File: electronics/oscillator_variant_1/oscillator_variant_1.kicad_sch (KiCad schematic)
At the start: 48 parts, among them J1 module_2x15_left_input, J2 module_2x15_right_input, J3 Coax, Q1 BC337, U1 TL081, U2 LME49720, U3 TL082, U4 TL431

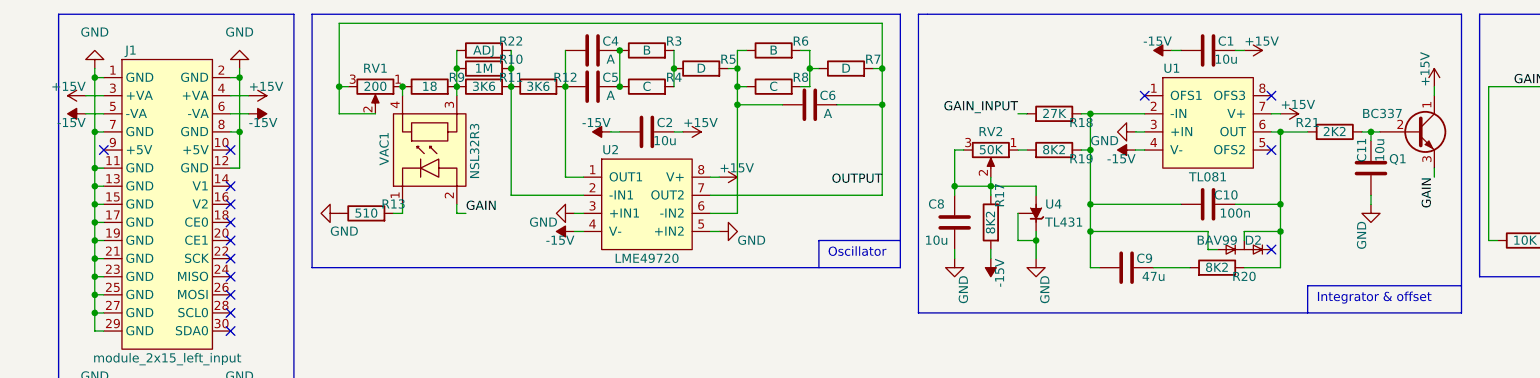
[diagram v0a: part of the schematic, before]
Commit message: placing and routing in progress, changed some ordering of resistors
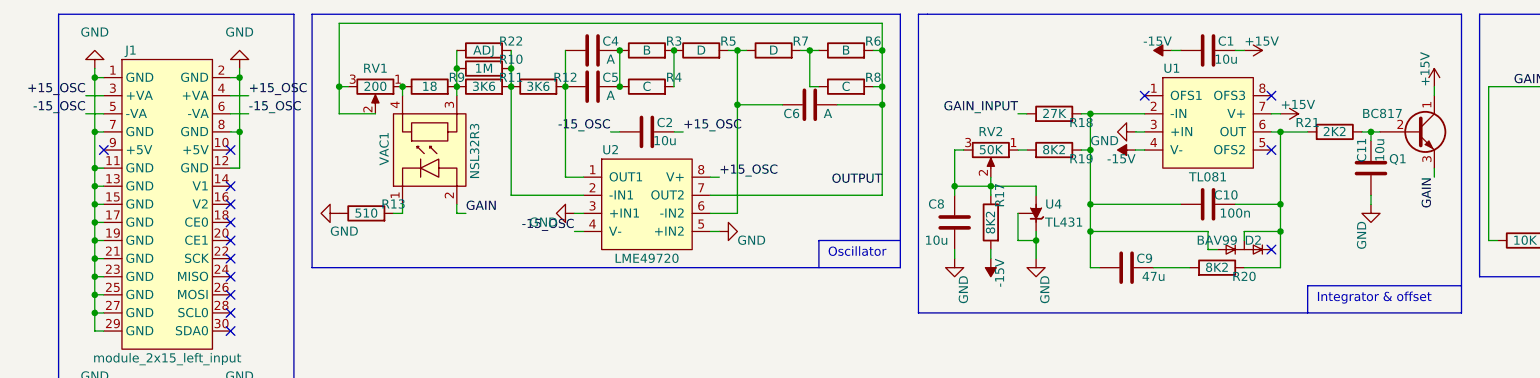
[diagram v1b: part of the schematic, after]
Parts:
- C10, C9: footprint SquantorRcl:C-025_050-030X100-film -> SquantorRcl:C-050-030X100-film
- C4, C5, C6: footprint SquantorRcl:C-025_050-030X100-film -> SquantorRcl:C-025_050-050X100-0805-3516-film
- Q1: value BC337 -> BC817; footprint Package_TO_SOT_THT:TO-92L_Inline_Wide -> SquantorIC:SOT23-3
- RV2: footprint Potentiometer_THT:Potentiometer_Bourns_3296W_Vertical -> SquantorRcl:POT_ALPS_RK09K111
- U4: footprint Package_TO_SOT_THT:TO-92_Inline_Wide -> SquantorIC:SOT23-3
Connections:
- net +15V: no longer C2.2, J1.3 (+VA), J1.4 (+VA), U2.8 (V+)
- net -15V: no longer C2.1, J1.5 (-VA), J1.6 (-VA), U2.4 (V-)
- net OUTPUT: now also R6.2, R8.2; no longer R7.2
- net at C6.1, R5.2, U2.6 (-IN2): now also R7.1; no longer R6.1, R8.1
- new net: R6.1, R7.2, R8.1
- new net +15_OSC: C2.2, J1.3 (+VA), J1.4 (+VA), U2.8 (V+)
- new net -15_OSC: C2.1, J1.5 (-VA), J1.6 (-VA), U2.4 (V-)
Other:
- moved on the sheet: R5, R6, R7, R8

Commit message: placing and routing further
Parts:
- R1, R13, R14, R15, R16, R17, R18, R19, R2, R20, R21: footprint SquantorRcl:R_0805+0603 -> SquantorRcl:R_0603_hand
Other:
- note added: "Power flags"
- note added: "interfaces"
- moved on the sheet: J3, R1, R2

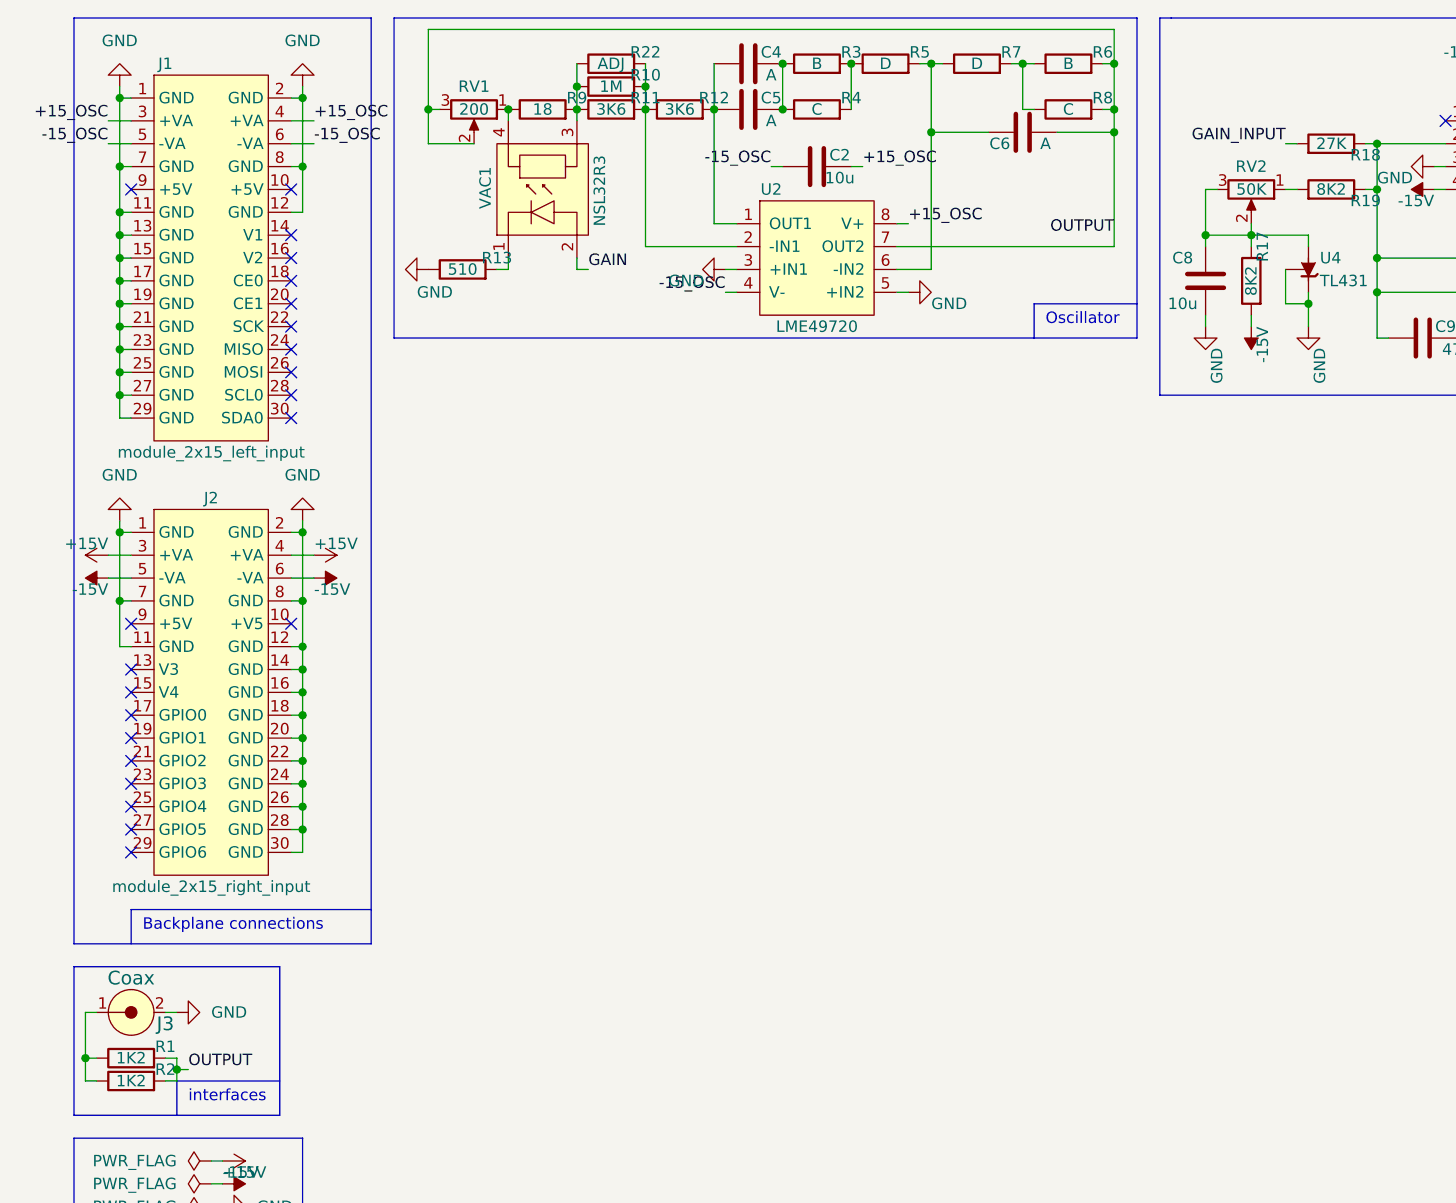
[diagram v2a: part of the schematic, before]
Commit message: updated some shielded components, changing routing of some nets keeping the ground plane as much contigious as possible
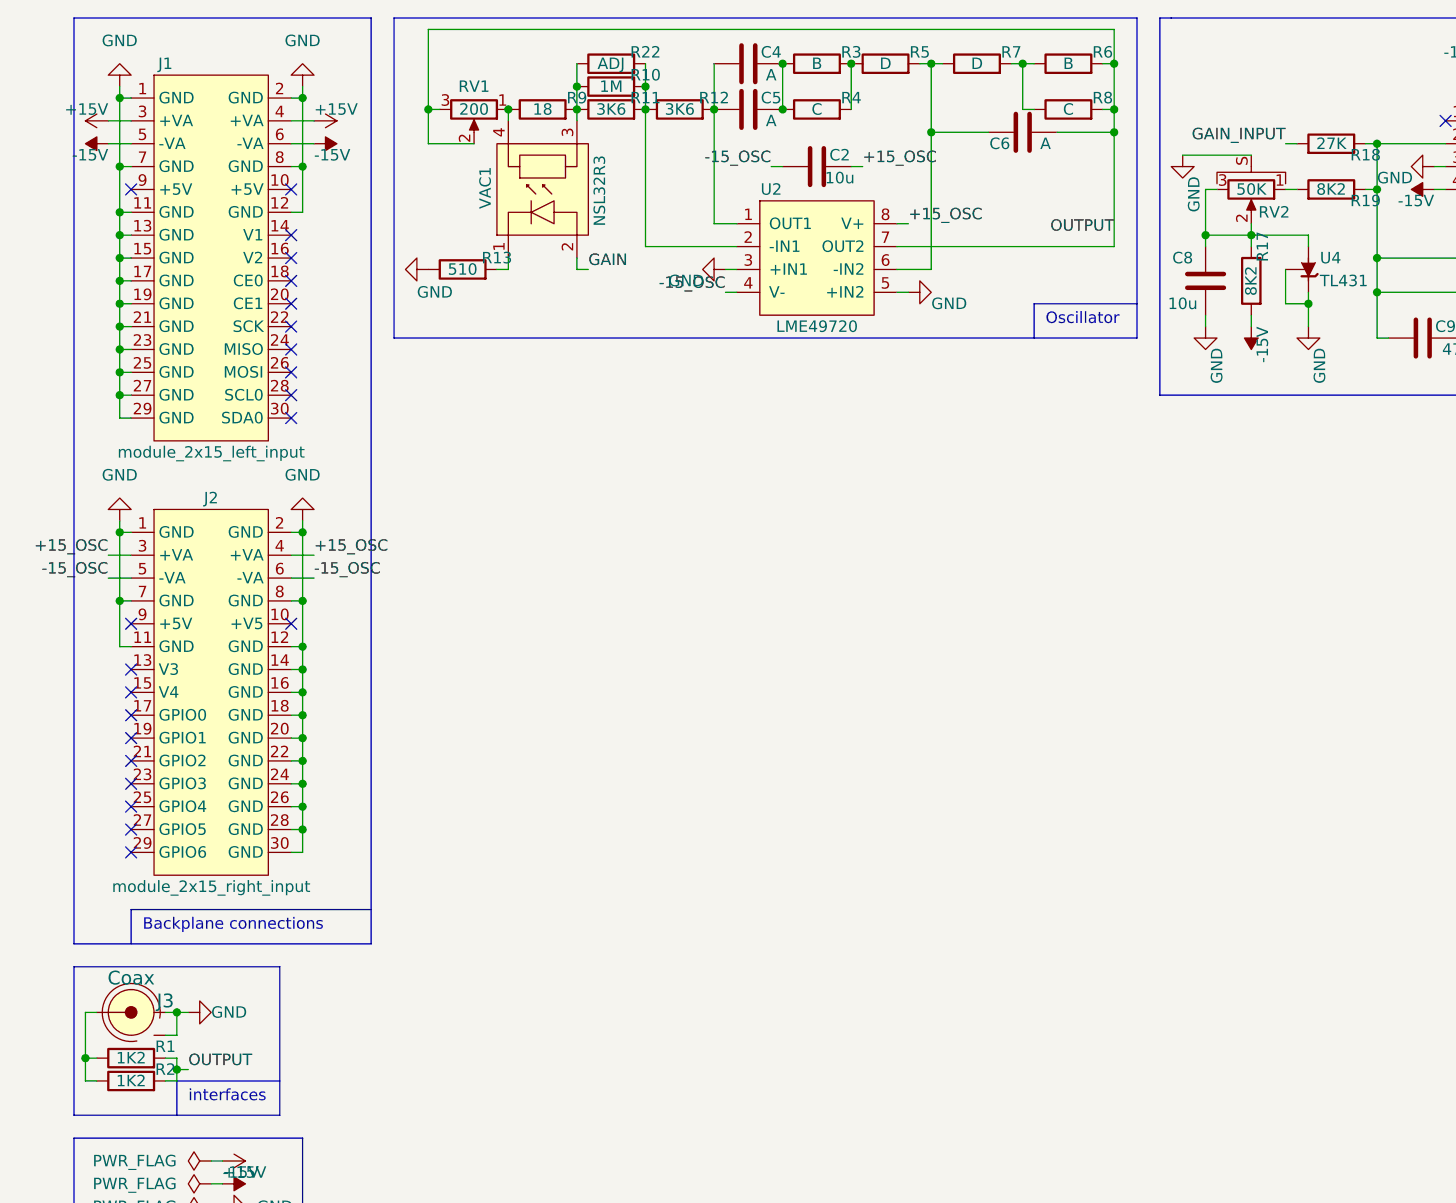
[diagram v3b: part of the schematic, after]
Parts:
- J3: symbol SquantorConnectors:Coax -> SquantorConnectors:Coax_with_shield
- RV2: symbol Device:R_Potentiometer -> SquantorDevice:R_Potentiometer_shielded
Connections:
- net +15V: now also J1.3 (+VA), J1.4 (+VA); no longer J2.3 (+VA), J2.4 (+VA)
- net +15_OSC: now also J2.3 (+VA), J2.4 (+VA); no longer J1.3 (+VA), J1.4 (+VA)
- net -15V: now also J1.5 (-VA), J1.6 (-VA); no longer J2.5 (-VA), J2.6 (-VA)
- net -15_OSC: now also J2.5 (-VA), J2.6 (-VA); no longer J1.5 (-VA), J1.6 (-VA)
- net GND: now also J3.S, RV2.S (shield)
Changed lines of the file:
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@@
   (junction (at 185.42 44.45) (diameter 0) (color 0 0 0 0)
+  )
+  (junction (at 25.4 124.46) (diameter 0) (color 0 0 0 0)
   )
   (junction (at 224.79 45.72) (diameter 0) (color 0 0 0 0)
@@
     (stroke (width 0) (type default) (color 0 0 0 0))
   )
+  (wire (pts (xy 25.4 127) (xy 25.4 124.46))
+    (stroke (width 0) (type default) (color 0 0 0 0))
+  )
   (wire (pts (xy 19.05 45.72) (xy 19.05 48.26))
     (stroke (width 0) (type default) (color 0 0 0 0))
@@
     (stroke (width 0) (type default) (color 0 0 0 0))
   )
+  (wire (pts (xy 25.4 124.46) (xy 26.67 124.46))
+    (stroke (width 0) (type default) (color 0 0 0 0))
+  )
   (wire (pts (xy 19.05 53.34) (xy 20.32 53.34))
     (stroke (width 0) (type default) (color 0 0 0 0))
@@
     (stroke (width 0) (type default) (color 0 0 0 0))
   )
+  (wire (pts (xy 24.13 127) (xy 25.4 127))
+    (stroke (width 0) (type default) (color 0 0 0 0))
+  )
   (wire (pts (xy 38.1 78.74) (xy 39.37 78.74))
     (stroke (width 0) (type default) (color 0 0 0 0))
@@
   )
   (wire (pts (xy 19.05 78.74) (xy 19.05 71.12))
+    (stroke (width 0) (type default) (color 0 0 0 0))
+  )
+  (wire (pts (xy 137.16 29.21) (xy 144.78 29.21))
     (stroke (width 0) (type default) (color 0 0 0 0))
   )
@@
     (effects (font (size 1.27 1.27)) (justify right bottom))
   )
-  (label "+15_OSC" (at 17.78 25.4 180)
+  (label "+15_OSC" (at 17.78 73.66 180)
     (effects (font (size 1.27 1.27)) (justify right bottom))
   )
-  (label "-15_OSC" (at 17.78 27.94 180)
+  (label "-15_OSC" (at 17.78 76.2 180)
     (effects (font (size 1.27 1.27)) (justify right bottom))
   )
@@
     (effects (font (size 1.27 1.27)) (justify left bottom))
   )
-  (label "-15_OSC" (at 40.64 27.94 0)
+  (label "-15_OSC" (at 40.64 76.2 0)
     (effects (font (size 1.27 1.27)) (justify left bottom))
   )
-  (label "+15_OSC" (at 40.64 25.4 0)
+  (label "+15_OSC" (at 40.64 73.66 0)
     (effects (font (size 1.27 1.27)) (justify left bottom))
   )
@@
     (pin "1")
   )
-  (symbol (lib_id "power:-15V") (at 17.78 76.2 90) (mirror x) (unit 1)
-    (in_bom yes) (on_board yes)
-    (property "Reference" "#PWR04" (id 0) (at 15.24 76.2 0)
-      (effects (font (size 1.27 1.27)) hide)
-    )
-    (property "Value" "-15V" (id 1) (at 17.78 77.47 90)
-      (effects (font (size 1.27 1.27)) (justify left))
-    )
-    (property "Footprint" "" (id 2) (at 17.78 76.2 0)
-      (effects (font (size 1.27 1.27)) hide)
-    )
-    (property "Datasheet" "" (id 3) (at 17.78 76.2 0)
+  (symbol (lib_id "power:-15V") (at 17.78 27.94 90) (mirror x) (unit 1)
+    (in_bom yes) (on_board yes)
+    (property "Reference" "#PWR04" (id 0) (at 15.24 27.94 0)
+      (effects (font (size 1.27 1.27)) hide)
+    )
+    (property "Value" "-15V" (id 1) (at 17.78 29.21 90)
+      (effects (font (size 1.27 1.27)) (justify left))
+    )
+    (property "Footprint" "" (id 2) (at 17.78 27.94 0)
+      (effects (font (size 1.27 1.27)) hide)
+    )
+    (property "Datasheet" "" (id 3) (at 17.78 27.94 0)
       (effects (font (size 1.27 1.27)) hide)
     )
@@
     (pin "2")
   )
+  (symbol (lib_id "power:GND") (at 137.16 29.21 0) (unit 1)
+    (in_bom yes) (on_board yes)
+    (property "Reference" "#PWR?" (id 0) (at 137.16 35.56 0)
+      (effects (font (size 1.27 1.27)) hide)
+    )
+    (property "Value" "GND" (id 1) (at 138.43 35.56 90)
+      (effects (font (size 1.27 1.27)) (justify left))
+    )
+    (property "Footprint" "" (id 2) (at 137.16 29.21 0)
+      (effects (font (size 1.27 1.27)) hide)
+    )
+    (property "Datasheet" "" (id 3) (at 137.16 29.21 0)
+      (effects (font (size 1.27 1.27)) hide)
+    )
+    (pin "1")
+  )
   (symbol (lib_id "Device:R") (at 176.53 49.53 270) (mirror x) (unit 1)
     (in_bom yes) (on_board yes)
@@
     (pin "1")
   )
-  (symbol (lib_id "Device:R_Potentiometer") (at 144.78 33.02 270) (unit 1)
-    (in_bom yes) (on_board yes)
-    (property "Reference" "RV2" (id 0) (at 144.78 30.48 90))
+  (symbol (lib_id "SquantorDevice:R_Potentiometer_shielded") (at 144.78 33.02 270) (unit 1)
+    (in_bom yes) (on_board yes)
+    (property "Reference" "RV2" (id 0) (at 147.32 35.56 90))
     (property "Value" "50K" (id 1) (at 144.78 33.02 90))
     (property "Footprint" "SquantorRcl:POT_ALPS_RK09K111" (id 2) (at 144.78 33.02 0)
@@
     (pin "2")
     (pin "3")
+    (pin "S")
   )
   (symbol (lib_id "Device:R") (at 73.66 24.13 90) (unit 1)
@@
     (pin "1")
   )
-  (symbol (lib_id "power:+15V") (at 40.64 73.66 270) (unit 1)
-    (in_bom yes) (on_board yes)
-    (property "Reference" "#PWR07" (id 0) (at 36.83 73.66 0)
-      (effects (font (size 1.27 1.27)) hide)
-    )
-    (property "Value" "+15V" (id 1) (at 40.64 72.39 90)
-      (effects (font (size 1.27 1.27)) (justify left))
-    )
-    (property "Footprint" "" (id 2) (at 40.64 73.66 0)
-      (effects (font (size 1.27 1.27)) hide)
-    )
-    (property "Datasheet" "" (id 3) (at 40.64 73.66 0)
+  (symbol (lib_id "power:+15V") (at 40.64 25.4 270) (unit 1)
+    (in_bom yes) (on_board yes)
+    (property "Reference" "#PWR07" (id 0) (at 36.83 25.4 0)
+      (effects (font (size 1.27 1.27)) hide)
+    )
+    (property "Value" "+15V" (id 1) (at 40.64 24.13 90)
+      (effects (font (size 1.27 1.27)) (justify left))
+    )
+    (property "Footprint" "" (id 2) (at 40.64 25.4 0)
+      (effects (font (size 1.27 1.27)) hide)
+    )
+    (property "Datasheet" "" (id 3) (at 40.64 25.4 0)
       (effects (font (size 1.27 1.27)) hide)
     )
@@
     (pin "1")
   )
-  (symbol (lib_id "power:-15V") (at 40.64 76.2 270) (unit 1)
-    (in_bom yes) (on_board yes)
-    (property "Reference" "#PWR08" (id 0) (at 43.18 76.2 0)
-      (effects (font (size 1.27 1.27)) hide)
-    )
-    (property "Value" "-15V" (id 1) (at 40.64 77.47 90)
-      (effects (font (size 1.27 1.27)) (justify left))
-    )
-    (property "Footprint" "" (id 2) (at 40.64 76.2 0)
-      (effects (font (size 1.27 1.27)) hide)
-    )
-    (property "Datasheet" "" (id 3) (at 40.64 76.2 0)
+  (symbol (lib_id "power:-15V") (at 40.64 27.94 270) (unit 1)
+    (in_bom yes) (on_board yes)
+    (property "Reference" "#PWR08" (id 0) (at 43.18 27.94 0)
+      (effects (font (size 1.27 1.27)) hide)
+    )
+    (property "Value" "-15V" (id 1) (at 40.64 29.21 90)
+      (effects (font (size 1.27 1.27)) (justify left))
+    )
+    (property "Footprint" "" (id 2) (at 40.64 27.94 0)
+      (effects (font (size 1.27 1.27)) hide)
+    )
+    (property "Datasheet" "" (id 3) (at 40.64 27.94 0)
       (effects (font (size 1.27 1.27)) hide)
     )
@@
     (pin "1")
   )
-  (symbol (lib_id "power:GND") (at 25.4 124.46 90) (unit 1)
-    (in_bom yes) (on_board yes) (fields_autoplaced)
-    (property "Reference" "#PWR0106" (id 0) (at 31.75 124.46 0)
-      (effects (font (size 1.27 1.27)) hide)
-    )
-    (property "Value" "GND" (id 1) (at 29.21 124.4599 90)
+  (symbol (lib_id "power:GND") (at 26.67 124.46 90) (unit 1)
+    (in_bom yes) (on_board yes)
+    (property "Reference" "#PWR0106" (id 0) (at 33.02 124.46 0)
+      (effects (font (size 1.27 1.27)) hide)
+    )
+    (property "Value" "GND" (id 1) (at 29.21 124.46 90)
       (effects (font (size 1.27 1.27)) (justify right))
     )
-    (property "Footprint" "" (id 2) (at 25.4 124.46 0)
-      (effects (font (size 1.27 1.27)) hide)
-    )
-    (property "Datasheet" "" (id 3) (at 25.4 124.46 0)
+    (property "Footprint" "" (id 2) (at 26.67 124.46 0)
+      (effects (font (size 1.27 1.27)) hide)
+    )
+    (property "Datasheet" "" (id 3) (at 26.67 124.46 0)
       (effects (font (size 1.27 1.27)) hide)
     )
@@
     (pin "1")
   )
-  (symbol (lib_id "power:+15V") (at 17.78 73.66 90) (mirror x) (unit 1)
-    (in_bom yes) (on_board yes)
-    (property "Reference" "#PWR03" (id 0) (at 21.59 73.66 0)
-      (effects (font (size 1.27 1.27)) hide)
-    )
-    (property "Value" "+15V" (id 1) (at 17.78 72.39 90)
-      (effects (font (size 1.27 1.27)) (justify left))
-    )
-    (property "Footprint" "" (id 2) (at 17.78 73.66 0)
-      (effects (font (size 1.27 1.27)) hide)
-    )
-    (property "Datasheet" "" (id 3) (at 17.78 73.66 0)
+  (symbol (lib_id "power:+15V") (at 17.78 25.4 90) (mirror x) (unit 1)
+    (in_bom yes) (on_board yes)
+    (property "Reference" "#PWR03" (id 0) (at 21.59 25.4 0)
+      (effects (font (size 1.27 1.27)) hide)
+    )
+    (property "Value" "+15V" (id 1) (at 17.78 24.13 90)
+      (effects (font (size 1.27 1.27)) (justify left))
+    )
+    (property "Footprint" "" (id 2) (at 17.78 25.4 0)
+      (effects (font (size 1.27 1.27)) hide)
+    )
+    (property "Datasheet" "" (id 3) (at 17.78 25.4 0)
       (effects (font (size 1.27 1.27)) hide)
     )
@@
     (pin "1")
   )
-  (symbol (lib_id "SquantorConnectors:Coax") (at 20.32 124.46 0) (unit 1)
-    (in_bom yes) (on_board yes)
-    (property "Reference" "J3" (id 0) (at 24.13 125.73 0)
+  (symbol (lib_id "SquantorConnectors:Coax_with_shield") (at 20.32 124.46 0) (unit 1)
+    (in_bom yes) (on_board yes)
+    (property "Reference" "J3" (id 0) (at 24.13 123.19 0)
       (effects (font (size 1.524 1.524)))
     )
@@
     (pin "1")
     (pin "2")
+    (pin "S")
   )
   (symbol (lib_id "Device:R") (at 153.67 33.02 270) (mirror x) (unit 1)
@@
       (reference "#PWR0112") (unit 1) (value "GND") (footprint "")
     )
+    (path "/238ce11f-b0b3-469e-87f3-8391efcb6a56"
+      (reference "#PWR?") (unit 1) (value "GND") (footprint "")
+    )
     (path "/9becc288-ce01-4768-9828-7cceb055ae24"
